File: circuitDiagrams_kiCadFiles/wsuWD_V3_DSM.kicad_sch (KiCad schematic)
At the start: 46 parts, among them J1 MicroUSB, J2 Screw Terminal, U1 LD1086D2M33TR, U2 LD1086DT50TR, U3 TCAN332, U4 FT232RL, U5 ATmega644PA-AU, U6 ASDMB-16.000MHz-LC-T, U7 MAX7219, U8 MCP2515-xSO

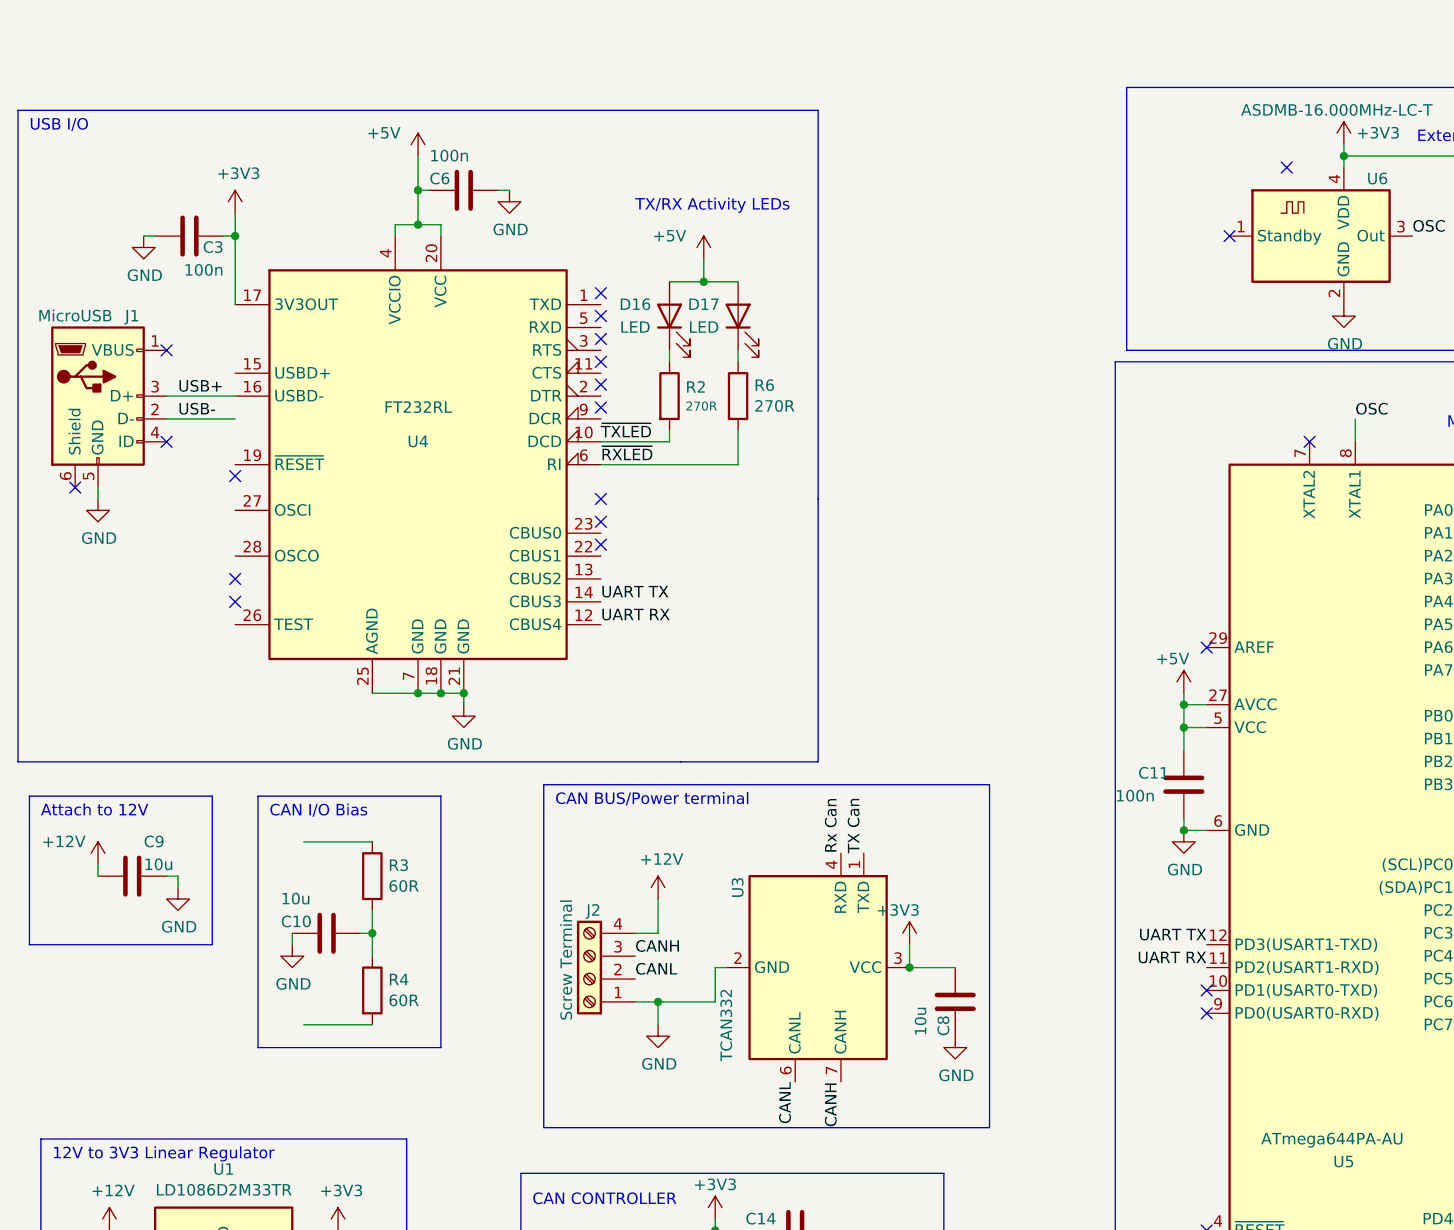
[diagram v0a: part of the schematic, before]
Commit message: Added USB A
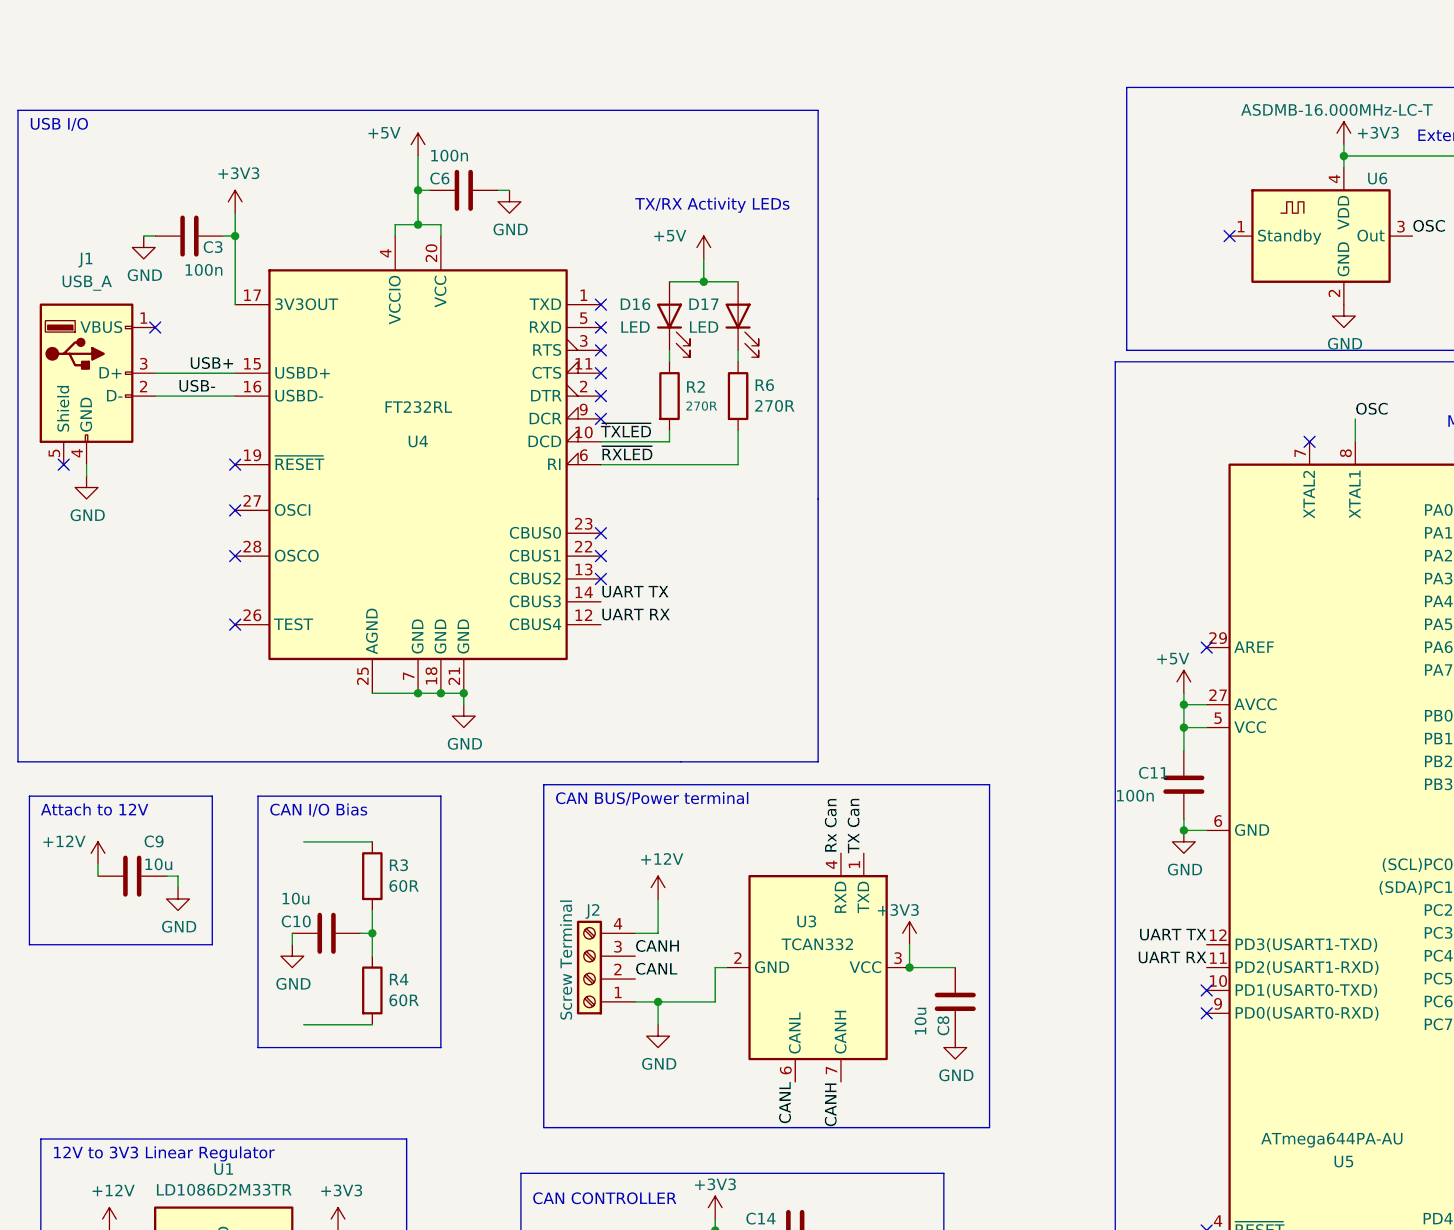
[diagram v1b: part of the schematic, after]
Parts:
- removed J1: MicroUSB, symbol Connector:USB_B_Micro
- added J1: USB_A, symbol Connector:USB_A
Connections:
- net GND: now also J1.4 (GND)
- net USB+: now also U4.15 (USBD+), J1.3 (D+); no longer U4.16 (USBD-)
- net USB-: now also U4.16 (USBD-), J1.2 (D-)
- no-connect marks 60 -> 59
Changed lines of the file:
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@@
   )
   (no_connect (at 180.34 91.44))
-  (no_connect (at 78.74 44.45))
+  (no_connect (at 78.74 45.72))
   (no_connect (at 180.34 88.9))
-  (no_connect (at 154.94 22.86))
   (no_connect (at 180.34 68.58))
-  (no_connect (at 78.74 41.91))
-  (no_connect (at 20.32 58.42))
-  (no_connect (at 30.48 53.34))
-  (no_connect (at 78.74 59.69))
+  (no_connect (at 78.74 43.18))
+  (no_connect (at 19.05 55.88))
+  (no_connect (at 38.1 55.88))
+  (no_connect (at 78.74 63.5))
   (no_connect (at 157.48 53.34))
   (no_connect (at 76.2 170.18))
@@
   (no_connect (at 146.05 140.97))
   (no_connect (at 180.34 60.96))
-  (no_connect (at 38.1 71.12))
+  (no_connect (at 38.1 73.66))
   (no_connect (at 180.34 78.74))
   (no_connect (at 180.34 107.95))
   (no_connect (at 148.59 30.48))
   (no_connect (at 180.34 73.66))
-  (no_connect (at 78.74 36.83))
+  (no_connect (at 78.74 38.1))
   (no_connect (at 146.05 114.3))
   (no_connect (at 146.05 116.84))
   (no_connect (at 180.34 115.57))
-  (no_connect (at 30.48 43.18))
-  (no_connect (at 78.74 62.23))
+  (no_connect (at 29.21 40.64))
+  (no_connect (at 78.74 66.04))
   (no_connect (at 180.34 71.12))
   (no_connect (at 180.34 66.04))
-  (no_connect (at 78.74 46.99))
+  (no_connect (at 78.74 48.26))
   (no_connect (at 180.34 63.5))
   (no_connect (at 180.34 110.49))
   (no_connect (at 163.83 154.94))
   (no_connect (at 180.34 113.03))
-  (no_connect (at 38.1 57.15))
+  (no_connect (at 38.1 66.04))
   (no_connect (at 106.68 180.34))
   (no_connect (at 106.68 177.8))
@@
   (no_connect (at 146.05 76.2))
   (no_connect (at 180.34 76.2))
-  (no_connect (at 38.1 68.58))
-  (no_connect (at 78.74 49.53))
-  (no_connect (at 78.74 39.37))
+  (no_connect (at 38.1 60.96))
+  (no_connect (at 78.74 50.8))
+  (no_connect (at 78.74 40.64))
   (no_connect (at 241.3 58.42))
   (no_connect (at 241.3 66.04))
@@
   (no_connect (at 241.3 73.66))
   (no_connect (at 180.34 86.36))
-  (no_connect (at 78.74 64.77))
+  (no_connect (at 78.74 68.58))
   (no_connect (at 180.34 118.11))
   (no_connect (at 180.34 105.41))
@@
     (stroke (width 0) (type default) (color 0 0 0 0))
   )
-  (wire (pts (xy 22.86 58.42) (xy 22.86 59.69))
+  (wire (pts (xy 21.59 55.88) (xy 21.59 57.15))
     (stroke (width 0) (type default) (color 0 0 0 0))
   )
@@
     (stroke (width 0) (type default) (color 0 0 0 0))
   )
-  (wire (pts (xy 38.1 50.8) (xy 30.48 50.8))
+  (wire (pts (xy 29.21 48.26) (xy 38.1 48.26))
     (stroke (width 0) (type default) (color 0 0 0 0))
   )
@@
     (stroke (width 0) (type default) (color 0 0 0 0))
   )
-  (wire (pts (xy 30.48 48.26) (xy 38.1 48.26))
+  (wire (pts (xy 29.21 45.72) (xy 38.1 45.72))
     (stroke (width 0) (type default) (color 0 0 0 0))
   )
@@
     (effects (font (size 1.27 1.27)) (justify right bottom))
   )
-  (label "USB+" (at 31.75 48.26 0)
+  (label "USB+" (at 33.02 45.72 0)
     (effects (font (size 1.27 1.27)) (justify left bottom))
   )
@@
     (effects (font (size 1.27 1.27)) (justify left bottom))
   )
-  (label "USB-" (at 31.75 50.8 0)
+  (label "USB-" (at 31.75 48.26 0)
     (effects (font (size 1.27 1.27)) (justify left bottom))
   )
@@
     (pin "9")
   )
-  (symbol (lib_id "Connector:USB_B_Micro") (at 22.86 48.26 0) (unit 1)
-    (in_bom yes) (on_board yes)
-    (property "Reference" "J1" (id 0) (at 26.67 39.37 0))
-    (property "Value" "MicroUSB" (id 1) (at 20.32 39.37 0))
-    (property "Footprint" "" (id 2) (at 26.67 49.53 0)
-      (effects (font (size 1.27 1.27)) hide)
-    )
-    (property "Datasheet" "~" (id 3) (at 26.67 49.53 0)
-      (effects (font (size 1.27 1.27)) hide)
-    )
-    (pin "1")
-    (pin "2")
-    (pin "3")
-    (pin "4")
-    (pin "5")
-    (pin "6")
-  )
   (symbol (lib_id "Regulator_Linear:LD1086D2M33TR") (at 36.83 143.51 0) (unit 1)
     (in_bom yes) (on_board yes)
@@
   (symbol (lib_id "Interface_CAN_LIN:TCAN332") (at 102.87 111.76 270) (unit 1)
     (in_bom yes) (on_board yes)
-    (property "Reference" "U3" (id 0) (at 93.98 102.87 0))
-    (property "Value" "TCAN332" (id 1) (at 92.71 118.11 0))
+    (property "Reference" "U3" (id 0) (at 101.6 106.68 90))
+    (property "Value" "TCAN332" (id 1) (at 102.87 109.22 90))
     (property "Footprint" "" (id 2) (at 99.06 127 90)
       (effects (font (size 1.27 1.27) italic) hide)
@@
     (pin "1")
   )
-  (symbol (lib_id "power:GND") (at 22.86 59.69 0) (unit 1)
-    (in_bom yes) (on_board yes)
-    (property "Reference" "#PWR0102" (id 0) (at 22.86 66.04 0)
-      (effects (font (size 1.27 1.27)) hide)
-    )
-    (property "Value" "GND" (id 1) (at 22.987 64.0842 0))
-    (property "Footprint" "" (id 2) (at 22.86 59.69 0)
-      (effects (font (size 1.27 1.27)) hide)
-    )
-    (property "Datasheet" "" (id 3) (at 22.86 59.69 0)
+  (symbol (lib_id "power:GND") (at 21.59 57.15 0) (unit 1)
+    (in_bom yes) (on_board yes)
+    (property "Reference" "#PWR0102" (id 0) (at 21.59 63.5 0)
+      (effects (font (size 1.27 1.27)) hide)
+    )
+    (property "Value" "GND" (id 1) (at 21.717 61.5442 0))
+    (property "Footprint" "" (id 2) (at 21.59 57.15 0)
+      (effects (font (size 1.27 1.27)) hide)
+    )
+    (property "Datasheet" "" (id 3) (at 21.59 57.15 0)
       (effects (font (size 1.27 1.27)) hide)
     )
@@
     (pin "2")
   )
+  (symbol (lib_id "Connector:USB_A") (at 21.59 45.72 0) (unit 1)
+    (in_bom yes) (on_board yes) (fields_autoplaced)
+    (property "Reference" "J1" (id 0) (at 21.59 33.02 0))
+    (property "Value" "USB_A" (id 1) (at 21.59 35.56 0))
+    (property "Footprint" "" (id 2) (at 25.4 46.99 0)
+      (effects (font (size 1.27 1.27)) hide)
+    )
+    (property "Datasheet" " ~" (id 3) (at 25.4 46.99 0)
+      (effects (font (size 1.27 1.27)) hide)
+    )
+    (pin "1")
+    (pin "2")
+    (pin "3")
+    (pin "4")
+    (pin "5")
+  )
   (symbol (lib_id "power:GND") (at 91.44 185.42 0) (unit 1)
     (in_bom yes) (on_board yes) (fields_autoplaced)
@@
       (reference "D17") (unit 1) (value "LED") (footprint "")
     )
-    (path "/00000000-0000-0000-0000-00006010c6ca"
-      (reference "J1") (unit 1) (value "MicroUSB") (footprint "")
+    (path "/c03374e9-87ea-401d-8ec8-f0596c74ecdf"
+      (reference "J1") (unit 1) (value "USB_A") (footprint "")
     )
     (path "/00000000-0000-0000-0000-00006012d7e2"
